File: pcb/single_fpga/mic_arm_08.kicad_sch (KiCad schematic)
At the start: 18 parts, among them U73 IM72D128V01XTMA1, U74 IM72D128V01XTMA1, U75 IM72D128V01XTMA1, U76 IM72D128V01XTMA1, U77 IM72D128V01XTMA1, U78 IM72D128V01XTMA1, U79 IM72D128V01XTMA1, U80 IM72D128V01XTMA1, U81 CDCLVC1108PW

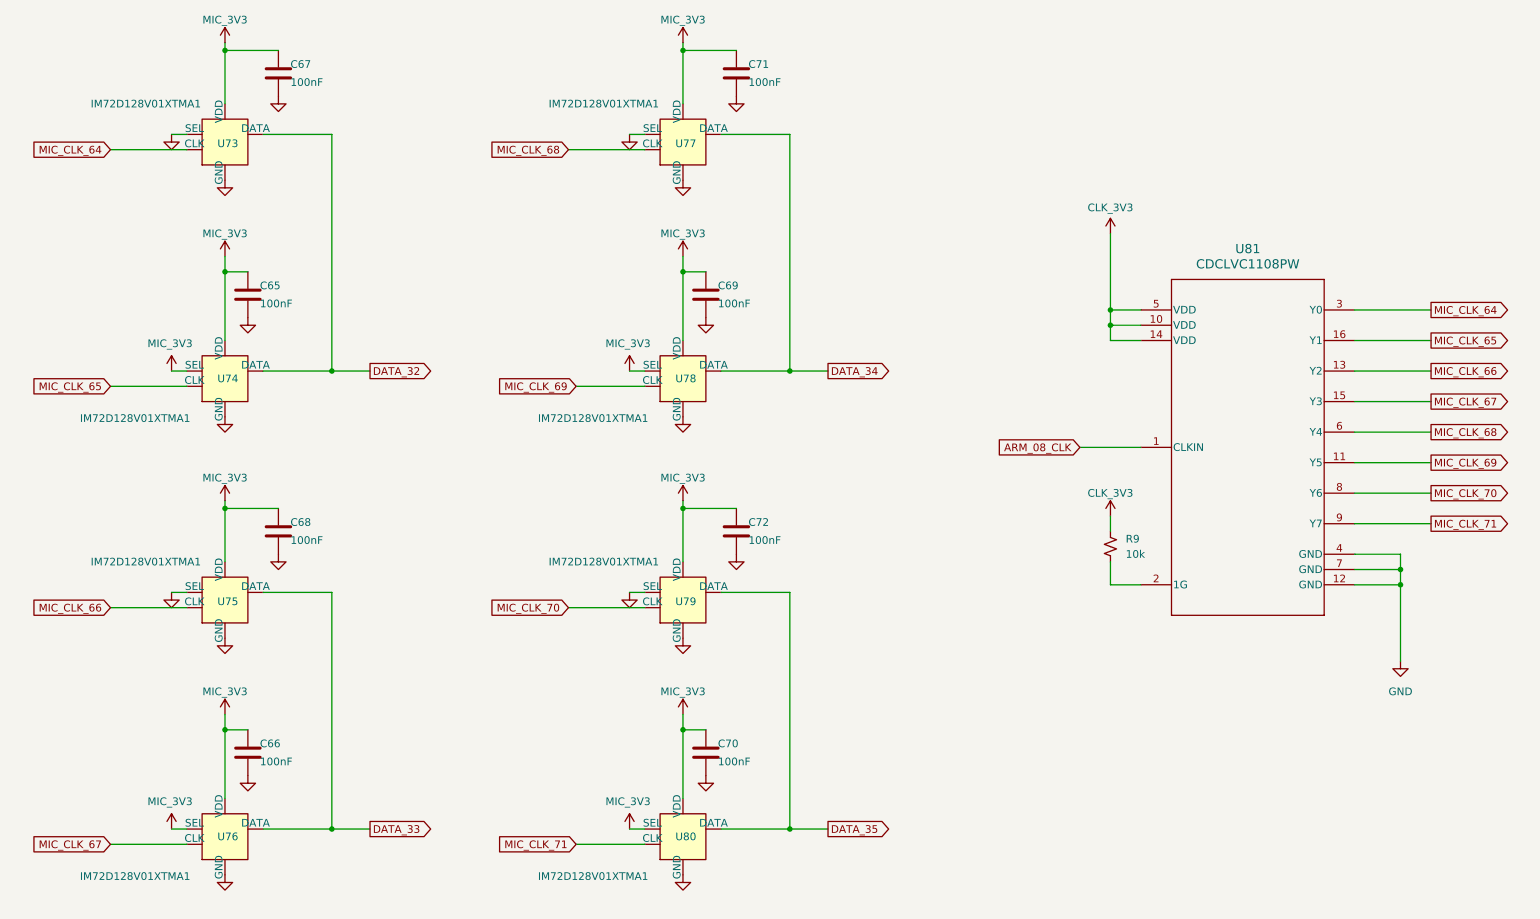
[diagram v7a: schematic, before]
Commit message: Changed mic symbol to improve readability.
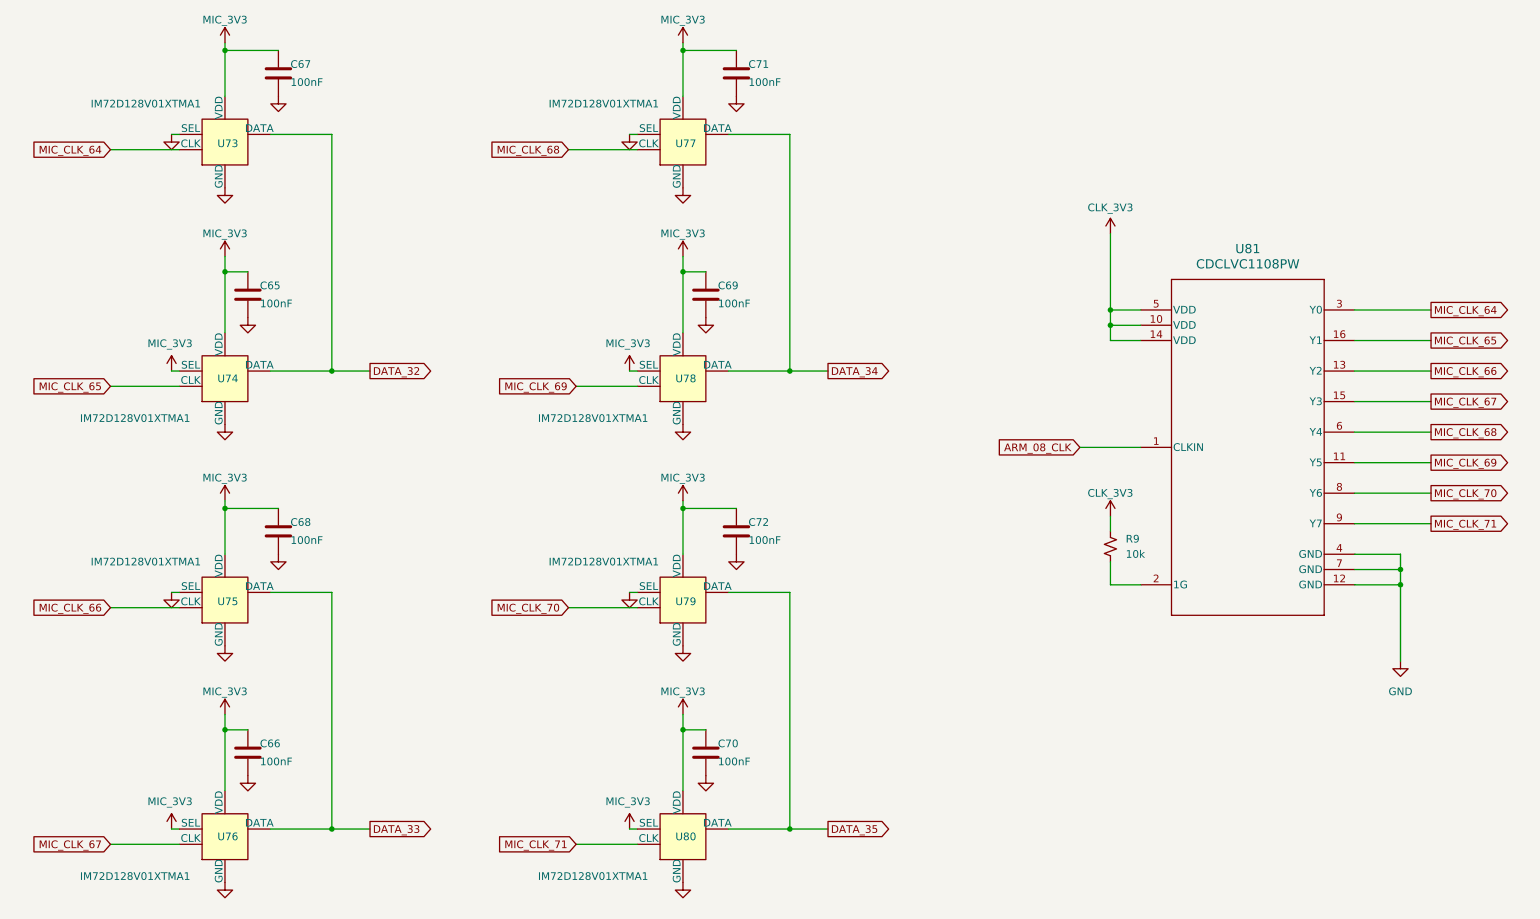
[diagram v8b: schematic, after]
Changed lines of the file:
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@@
 	(wire
 		(pts
-			(xy 153.67 119.38) (xy 142.24 119.38)
+			(xy 153.67 119.38) (xy 143.51 119.38)
 		)
 		(stroke
@@
 	(wire
 		(pts
-			(xy 40.64 161.29) (xy 53.34 161.29)
+			(xy 40.64 161.29) (xy 52.07 161.29)
 		)
 		(stroke
@@
 	(wire
 		(pts
-			(xy 50.8 43.18) (xy 53.34 43.18)
+			(xy 50.8 43.18) (xy 52.07 43.18)
 		)
 		(stroke
@@
 	(wire
 		(pts
-			(xy 40.64 121.92) (xy 53.34 121.92)
+			(xy 40.64 121.92) (xy 52.07 121.92)
 		)
 		(stroke
@@
 	(wire
 		(pts
-			(xy 135.89 66.04) (xy 135.89 77.47)
+			(xy 135.89 66.04) (xy 135.89 76.2)
 		)
 		(stroke
@@
 	(wire
 		(pts
-			(xy 66.04 158.75) (xy 77.47 158.75)
+			(xy 67.31 158.75) (xy 77.47 158.75)
 		)
 		(stroke
@@
 	(wire
 		(pts
-			(xy 127 119.38) (xy 129.54 119.38)
+			(xy 127 119.38) (xy 128.27 119.38)
 		)
 		(stroke
@@
 	(wire
 		(pts
-			(xy 66.04 82.55) (xy 77.47 82.55)
+			(xy 67.31 82.55) (xy 77.47 82.55)
 		)
 		(stroke
@@
 	(wire
 		(pts
-			(xy 135.89 142.24) (xy 135.89 153.67)
+			(xy 135.89 142.24) (xy 135.89 152.4)
 		)
 		(stroke
@@
 	(wire
 		(pts
-			(xy 77.47 43.18) (xy 66.04 43.18)
+			(xy 77.47 43.18) (xy 67.31 43.18)
 		)
 		(stroke
@@
 	(wire
 		(pts
-			(xy 50.8 82.55) (xy 53.34 82.55)
+			(xy 50.8 82.55) (xy 52.07 82.55)
 		)
 		(stroke
@@
 	(wire
 		(pts
-			(xy 116.84 45.72) (xy 129.54 45.72)
+			(xy 116.84 45.72) (xy 128.27 45.72)
 		)
 		(stroke
@@
 	(wire
 		(pts
-			(xy 59.69 142.24) (xy 59.69 153.67)
+			(xy 59.69 142.24) (xy 59.69 152.4)
 		)
 		(stroke
@@
 	(wire
 		(pts
-			(xy 118.11 85.09) (xy 129.54 85.09)
+			(xy 118.11 85.09) (xy 128.27 85.09)
 		)
 		(stroke
@@
 	(wire
 		(pts
-			(xy 118.11 161.29) (xy 129.54 161.29)
+			(xy 118.11 161.29) (xy 128.27 161.29)
 		)
 		(stroke
@@
 	(wire
 		(pts
-			(xy 40.64 45.72) (xy 53.34 45.72)
+			(xy 40.64 45.72) (xy 52.07 45.72)
 		)
 		(stroke
@@
 	(wire
 		(pts
-			(xy 142.24 158.75) (xy 153.67 158.75)
+			(xy 143.51 158.75) (xy 153.67 158.75)
 		)
 		(stroke
@@
 	(wire
 		(pts
-			(xy 40.64 85.09) (xy 53.34 85.09)
+			(xy 40.64 85.09) (xy 52.07 85.09)
 		)
 		(stroke
@@
 	(wire
 		(pts
-			(xy 135.89 105.41) (xy 135.89 114.3)
+			(xy 135.89 105.41) (xy 135.89 113.03)
 		)
 		(stroke
@@
 	(wire
 		(pts
-			(xy 127 82.55) (xy 129.54 82.55)
+			(xy 127 82.55) (xy 128.27 82.55)
 		)
 		(stroke
@@
 	(wire
 		(pts
-			(xy 116.84 121.92) (xy 129.54 121.92)
+			(xy 116.84 121.92) (xy 128.27 121.92)
 		)
 		(stroke
@@
 	(wire
 		(pts
-			(xy 59.69 66.04) (xy 59.69 77.47)
+			(xy 59.69 66.04) (xy 59.69 76.2)
 		)
 		(stroke
@@
 	(wire
 		(pts
-			(xy 127 158.75) (xy 129.54 158.75)
+			(xy 127 158.75) (xy 128.27 158.75)
 		)
 		(stroke
@@
 	(wire
 		(pts
-			(xy 153.67 43.18) (xy 142.24 43.18)
+			(xy 153.67 43.18) (xy 143.51 43.18)
 		)
 		(stroke
@@
 	(wire
 		(pts
-			(xy 50.8 158.75) (xy 53.34 158.75)
+			(xy 50.8 158.75) (xy 52.07 158.75)
 		)
 		(stroke
@@
 	(wire
 		(pts
-			(xy 127 43.18) (xy 129.54 43.18)
+			(xy 127 43.18) (xy 128.27 43.18)
 		)
 		(stroke
@@
 	(wire
 		(pts
-			(xy 59.69 105.41) (xy 59.69 114.3)
+			(xy 59.69 105.41) (xy 59.69 113.03)
 		)
 		(stroke
@@
 	(wire
 		(pts
-			(xy 135.89 29.21) (xy 135.89 38.1)
+			(xy 135.89 29.21) (xy 135.89 36.83)
 		)
 		(stroke
@@
 	(wire
 		(pts
-			(xy 50.8 119.38) (xy 53.34 119.38)
+			(xy 50.8 119.38) (xy 52.07 119.38)
 		)
 		(stroke
@@
 	(wire
 		(pts
-			(xy 59.69 29.21) (xy 59.69 38.1)
+			(xy 59.69 29.21) (xy 59.69 36.83)
 		)
 		(stroke
@@
 	(wire
 		(pts
-			(xy 77.47 119.38) (xy 66.04 119.38)
+			(xy 77.47 119.38) (xy 67.31 119.38)
 		)
 		(stroke
@@
 	(wire
 		(pts
-			(xy 142.24 82.55) (xy 153.67 82.55)
+			(xy 143.51 82.55) (xy 153.67 82.55)
 		)
 		(stroke
@@
 	(symbol
 		(lib_id "power:GND")
-		(at 135.89 166.37 0)
+		(at 135.89 167.64 0)
 		(unit 1)
 		(body_style 1)
@@
 	(symbol
 		(lib_id "power:GND")
-		(at 59.69 127 0)
+		(at 59.69 128.27 0)
 		(unit 1)
 		(body_style 1)
@@
 	(symbol
 		(lib_id "power:GND")
-		(at 59.69 90.17 0)
+		(at 59.69 91.44 0)
 		(unit 1)
 		(body_style 1)
@@
 	(symbol
 		(lib_id "power:GND")
-		(at 135.89 127 0)
+		(at 135.89 128.27 0)
 		(unit 1)
 		(body_style 1)
@@
 	(symbol
 		(lib_id "power:GND")
-		(at 135.89 50.8 0)
+		(at 135.89 52.07 0)
 		(unit 1)
 		(body_style 1)
@@
 	(symbol
 		(lib_id "power:GND")
-		(at 59.69 166.37 0)
+		(at 59.69 167.64 0)
 		(unit 1)
 		(body_style 1)
@@
 	(symbol
 		(lib_id "power:GND")
-		(at 135.89 90.17 0)
+		(at 135.89 91.44 0)
 		(unit 1)
 		(body_style 1)
@@
 	(symbol
 		(lib_id "power:GND")
-		(at 59.69 50.8 0)
+		(at 59.69 52.07 0)
 		(unit 1)
 		(body_style 1)
